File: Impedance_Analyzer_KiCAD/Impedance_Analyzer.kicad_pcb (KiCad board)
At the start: 2 copper layers, 94.4 x 90 mm, 70 parts, among them J1 Conn_Coaxial, J10 Conn_Coaxial, J11 Screw_Terminal_01x03, J2 Conn_Coaxial, J3 Conn_Coaxial, J4 Conn_Coaxial, J5 Conn_Coaxial, J6 Conn_Coaxial, J7 Conn_Coaxial, J8 Barrel_Jack_Switch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

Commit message: Formatting, Minor fixes
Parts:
- C10, C5, C8: value C -> 100n
- C4, C6: value CP -> 22u
- moved C9 5.00 mm to (135.0, 127.0), turned to 0 degrees
- turned R7 to 0 degrees
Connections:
- net Net-(BUF2-Pad6) renamed IMon+
- net Net-(J7-Pad1) renamed IMon-
- BUF1 pad 2: Net-(BUF1-Pad2) -> unconnected-(BUF1-Pad2)
- BUF1 pad 5: Net-(BUF1-Pad5) -> unconnected-(BUF1-Pad5)
- BUF1 pad 7: Net-(BUF1-Pad7) -> unconnected-(BUF1-Pad7)
- BUF2 pad 2: Net-(BUF2-Pad2) -> unconnected-(BUF2-Pad2)
- BUF2 pad 5: Net-(BUF2-Pad5) -> unconnected-(BUF2-Pad5)
- BUF2 pad 7: Net-(BUF2-Pad7) -> unconnected-(BUF2-Pad7)
- C9 pad 1: GND -> +5VP
- C9 pad 2: +5VP -> GND
- R7 pad 2: Net-(R7-Pad2) -> Net-(U3-Pad1)
- U3 pad 1: Net-(R7-Pad1) -> Net-(U3-Pad1)
- U3 pad 8: Net-(R7-Pad2) -> Net-(R7-Pad1)
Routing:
- net Net-(R7-Pad2): track 4.21 -> 0.00 mm
- net Net-(U3-Pad1): track 0.00 -> 4.16 mm
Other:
- net class Default removed

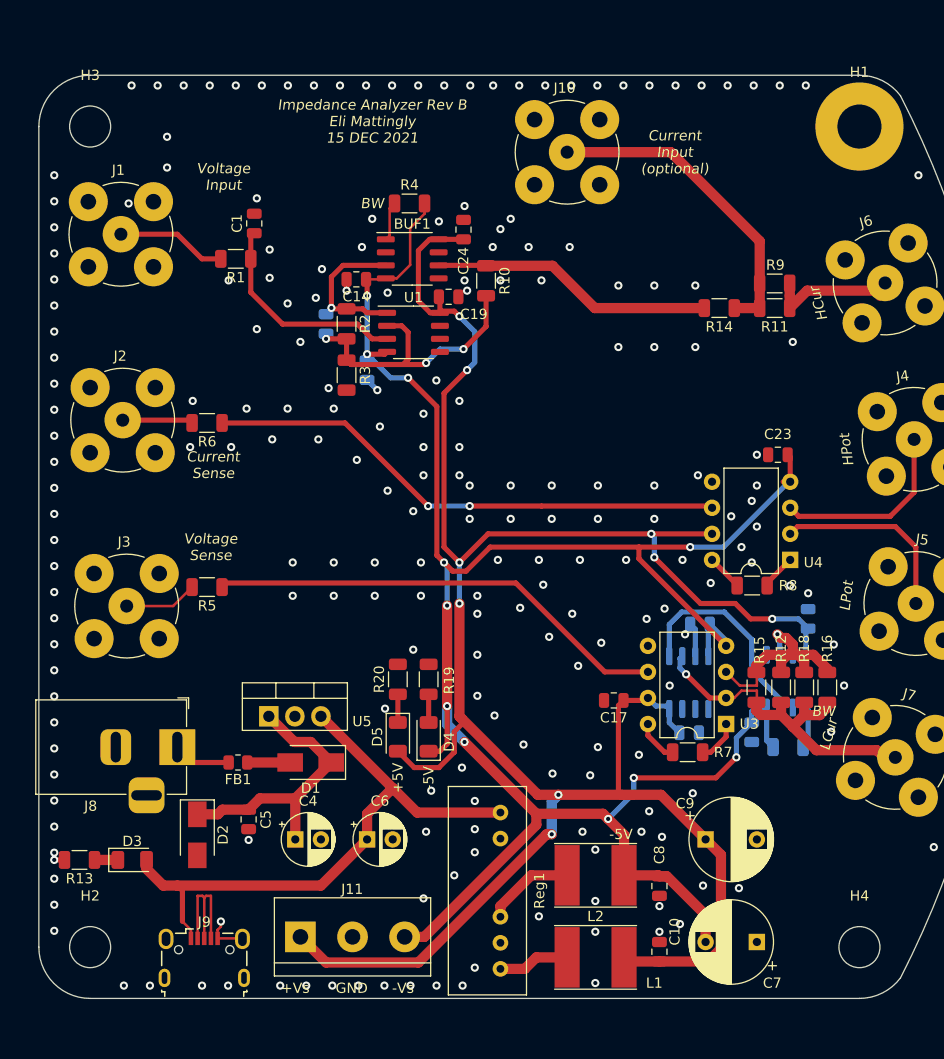
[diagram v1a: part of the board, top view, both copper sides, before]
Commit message: Update LTSPICE, Minor board changes
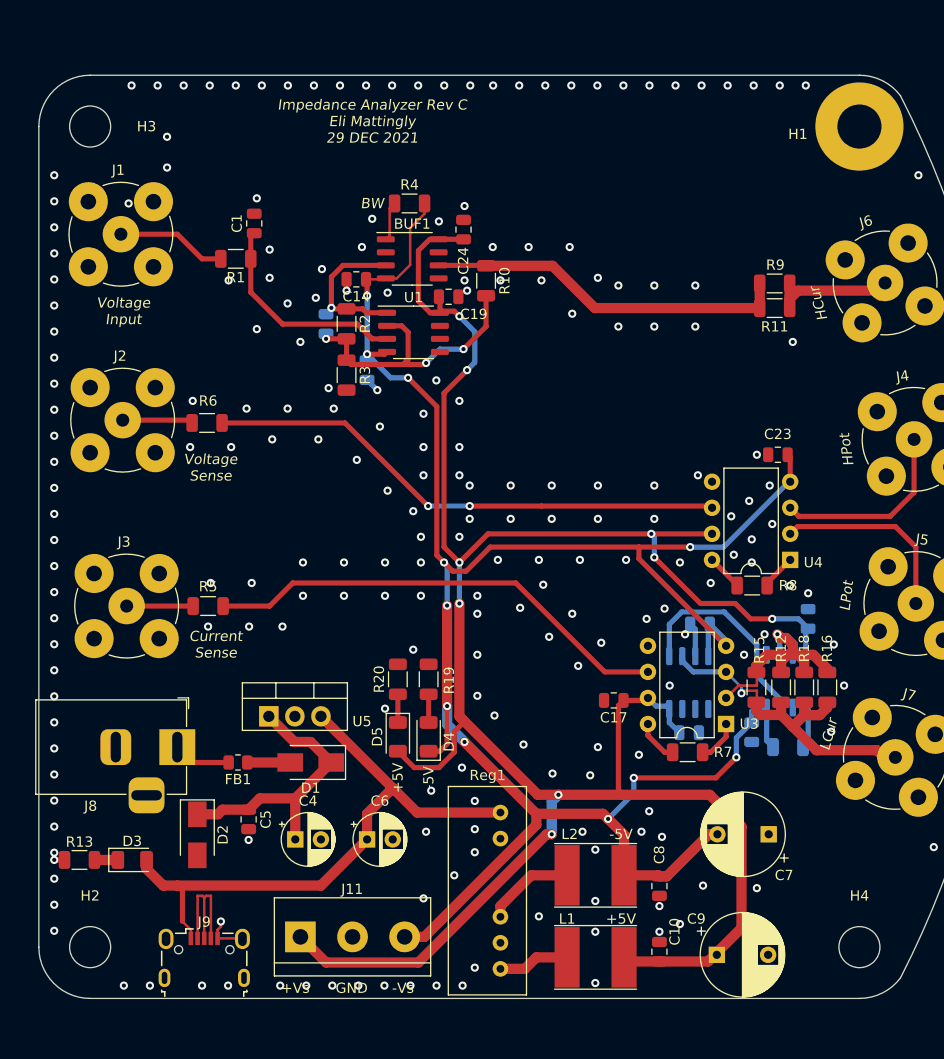
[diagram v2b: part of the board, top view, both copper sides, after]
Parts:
- removed J10: Conn_Coaxial, Connector_Coaxial:BNC_TEConnectivity_1478204_Vertical
- removed R14: 0, Resistor_SMD:R_1206_3216Metric
- moved C9 11.3 mm to (136.1, 138.2)
- moved C7 10.6 mm to (141.2, 126.5)
- moved R5 1.85 mm to (86.5, 104.2)
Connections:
- BUF2 pad 6: IMon+ -> IMon-
- J7 pad 1: IMon- -> IMon+
- R11 pad 2: Net-(R11-Pad2) -> Net-(BUF1-Pad6)
- R12 pad 1: IMon+ -> IMon-
- R12 pad 2: IMon- -> IMon+
- R15 pad 1: IMon+ -> IMon-
- R15 pad 2: IMon- -> IMon+
- R16 pad 1: IMon+ -> IMon-
- R16 pad 2: IMon- -> IMon+
- R18 pad 1: IMon+ -> IMon-
- R18 pad 2: IMon- -> IMon+
- R9 pad 2: Net-(R11-Pad2) -> Net-(BUF1-Pad6)
- U2 pad 2: IMon- -> IMon+
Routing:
- net Net-(R11-Pad2): track 31.4 -> 0.00 mm
- net IMon-: track 35.0 -> 22.9 mm
- net IMon+: track 22.9 -> 34.3 mm
- net Net-(BUF1-Pad6): track 27.6 -> 35.4 mm
- net +5VP: track 219.2 -> 223.7 mm
- net -5V: track 211.0 -> 209.0 mm
- net Net-(J3-Pad1): track 7.70 -> 6.48 mm
- net Net-(R5-Pad1): track 45.3 -> 45.9 mm
- net IOut: track 14.1 -> 14.7 mm
- net GND: vias 217 -> 227
- net (no net): vias 1 -> 0
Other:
- board text added: "Impedance Analyzer Rev C Eli Mattingly 29 DEC 2021"
- board text removed: "Current Input (optional)"
- board text removed: "Impedance Analyzer Rev B Eli Mattingly 15 DEC 2021"

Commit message: Gerbers
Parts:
- removed C2: DNP, Capacitor_SMD:C_0805_2012Metric
- removed R11, R12, R15, R16: 100, Resistor_SMD:R_1206_3216Metric
- C1: value DNP -> 1n
- R1: value 0 -> 1k
- moved R2 17.5 mm to (117.0, 81.0), turned to 90 degrees
- moved C1 17.1 mm to (100.0, 81.5), turned to -90 degrees
- moved R3 14.5 mm to (114.5, 81.0)
- moved R1 12.7 mm to (100.0, 77.0), turned to 90 degrees
- moved R18 4.62 mm to (140.0, 112.0), turned to 90 degrees
- moved R9 1.04 mm to (142.5, 73.5)
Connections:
- R1 pad 2: Net-(J1-Pad1) -> Net-(R1-Pad2)
- R10 pad 2: Net-(C2-Pad2) -> Net-(R10-Pad2)
- R2 pad 2: Net-(C2-Pad2) -> Net-(R10-Pad2)
- R3 pad 1: Net-(C2-Pad2) -> Net-(R10-Pad2)
- U1 pad 1: Net-(BUF1-Pad3) -> Net-(R1-Pad2)
- U1 pad 2: Net-(C2-Pad2) -> Net-(R1-Pad2)
- U1 pad 3: Net-(C1-Pad1) -> Net-(J1-Pad1)
- U1 pad 5: (no net) -> Net-(C1-Pad1)
- U1 pad 6: (no net) -> Net-(R10-Pad2)
- U1 pad 7: (no net) -> Net-(BUF1-Pad3)
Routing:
- net Net-(C2-Pad2): track 28.4 -> 0.00 mm, vias 3 -> 0
- net Net-(J1-Pad1): track 10.7 -> 30.2 mm
- net Net-(R10-Pad2): track 0.00 -> 14.6 mm, vias 0 -> 1
- net Net-(BUF1-Pad3): track 15.4 -> 29.1 mm, vias 1 -> 4
- net IMon-: track 22.9 -> 10.5 mm
- net Net-(C1-Pad1): track 21.2 -> 12.9 mm
- net Net-(R1-Pad2): track 0.00 -> 7.02 mm
- net IOut: track 14.7 -> 10.2 mm
- net Net-(BUF1-Pad6): track 35.4 -> 33.1 mm
- net IMon+: track 34.3 -> 32.2 mm, vias 1 -> 0
- net GND: vias 227 -> 225
